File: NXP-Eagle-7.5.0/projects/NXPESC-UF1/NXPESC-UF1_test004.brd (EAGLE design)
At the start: 59.7 x 20.3 mm, 63 parts, among them J2 FLH1-03SZ-S3A-T, U1 MKV31F512VLL12-M, U10 PSMN1R4-30YLD, U11 PSMN1R4-30YLD, U12 PSMN1R4-30YLD, U13 PSMN1R4-30YLD, U2 MKV31F512VLH12-M, U8 PSMN1R4-30YLD, U9 PSMN1R4-30YLD

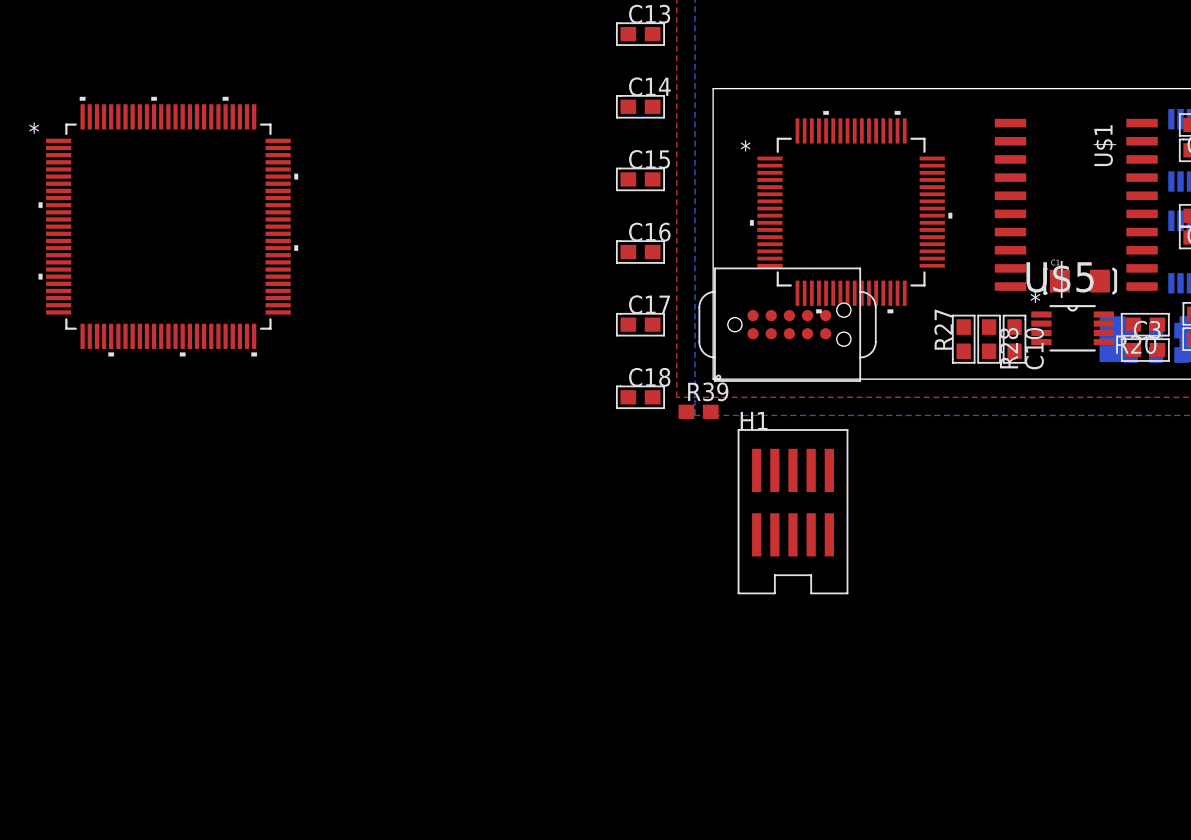
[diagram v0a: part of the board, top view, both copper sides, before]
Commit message: connected additional signals to gate driver
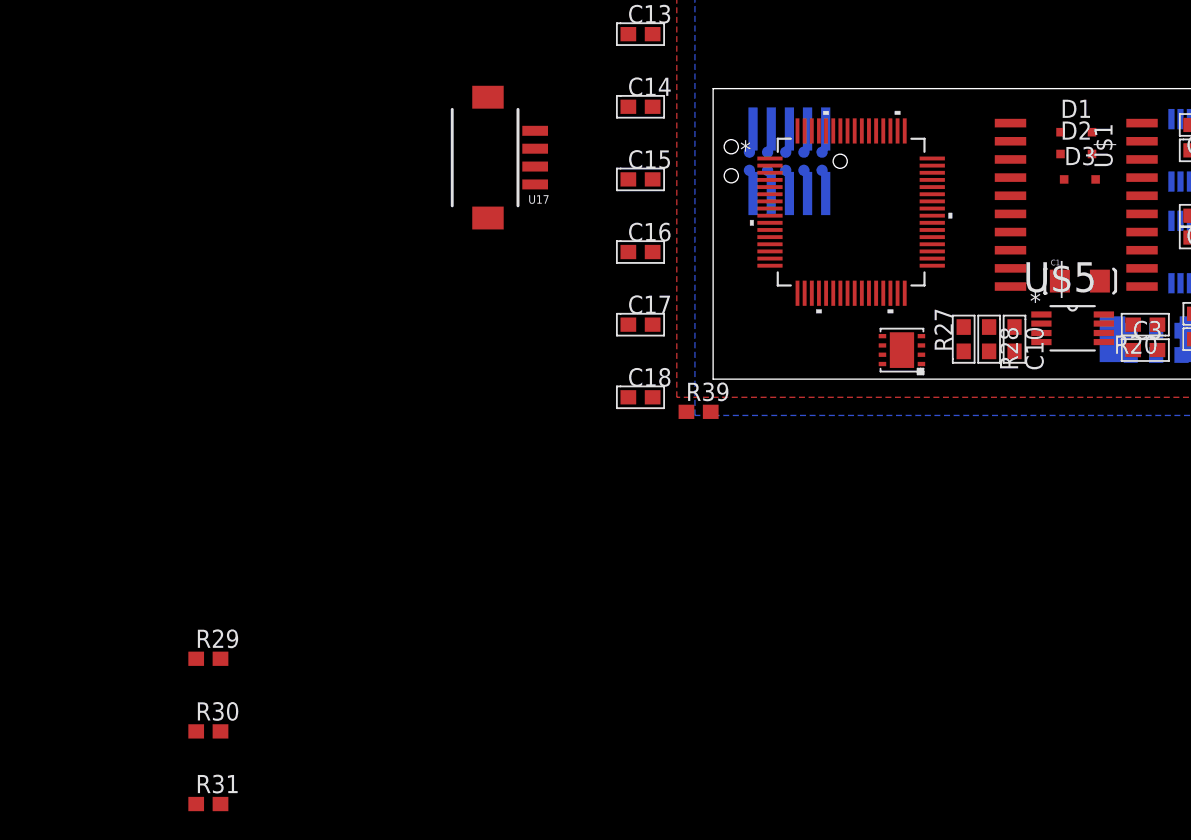
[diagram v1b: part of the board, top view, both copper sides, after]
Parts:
- removed U1: MKV31F512VLL12-M, MKV31F512VLL12:LQFP-100_14X14X1_7-M
- added D1, D2, D3: (no value), etc-diode_002a:SOD323-R
- added R29, R30, R31: RESC0603-100R, etc_rcl:C0603
- added U15: TJA1042TK/3, TJA1042T:HVSON8
- added U17: DF13-4P-1.25H, pixhawk2:DF13A-4P-1.25H
- C1: value (none) -> Find a 50V
- moved H1 23.9 mm to (5.33, 15.2), flipped to the bottom
- moved H3 13.6 mm to (8.89, 15.2), flipped to the bottom
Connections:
- net N$7 renamed PWM_BT
- net N$8 renamed PWM_BB
- removed net VB1: U$1.20
- removed net VB2: U$1.16
- removed net VB3: U$1.10
- removed net VDD_2: U2.30
- removed net VDD_3: U1.40, U2.48
- removed net VDD_7: U1.89
- removed net VSS_2: U2.31
- removed net VSS_3: U1.41
- removed net VSS_7: U1.88
- new net +5V: U15.3
- new net CAN0_RX: U15.4, U2.29
- new net CAN0_TX: U15.1, U2.28
- new net N$15: D3.C, U$1.20
- new net N$16: D2.C, U$1.16
- new net N$18: D1.C, U$1.10
- new net N$22: U15.7, U17.2
- new net N$23: U15.6, U17.3
- new net N$7: D3.A, R31.2
- new net N$8: R29.1, R30.1, R31.1
- new net PWM_AB: U$1.2, U2.45
- new net PWM_AT: U$1.1, U2.44
- new net PWM_CB: U$1.6, U2.62
- new net PWM_CT: U$1.5, U2.61
- new net STB: U15.8, U2.27
- net +3V3: now also U15.5, U2.30, U2.48; no longer U1.30, U1.48, U1.61, U1.75, U1.8, U2.20, U2.47
- net GND: now also U15.2, U17.4, U2.31, U2.47; no longer U1.29, U1.49, U1.60, U1.74, U1.9, U2.21, U2.32
- net N$5: now also D1.A, R29.2; no longer U$1.1, U1.71, U2.44
- net N$6: now also D2.A, R30.2; no longer U$1.2, U1.72, U2.45
- net VDDA: no longer U1.22
- net VREFH: no longer U1.23
- net VREFL: no longer U1.24
- net VSSA: no longer U1.25

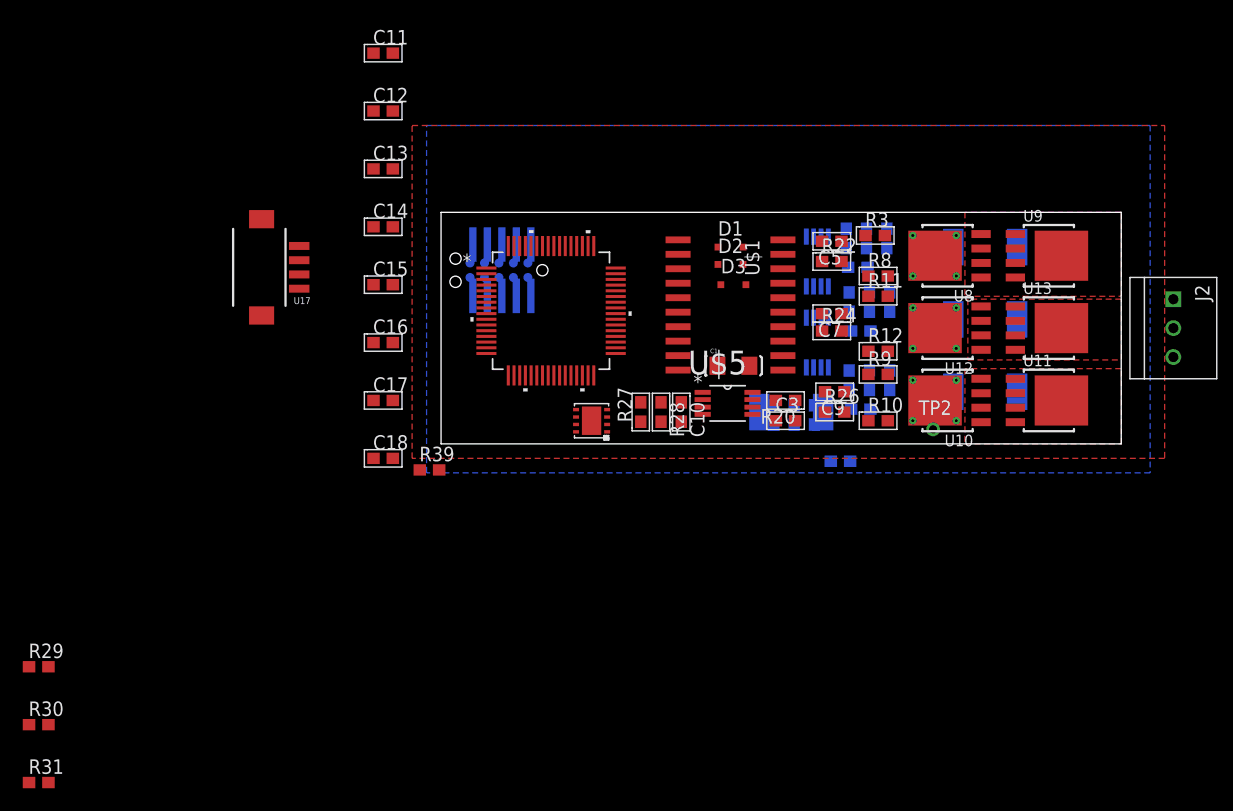
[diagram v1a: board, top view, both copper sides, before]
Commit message: moved from rev 003 to 004, merged in Gallowaa CAN conenctor additions.
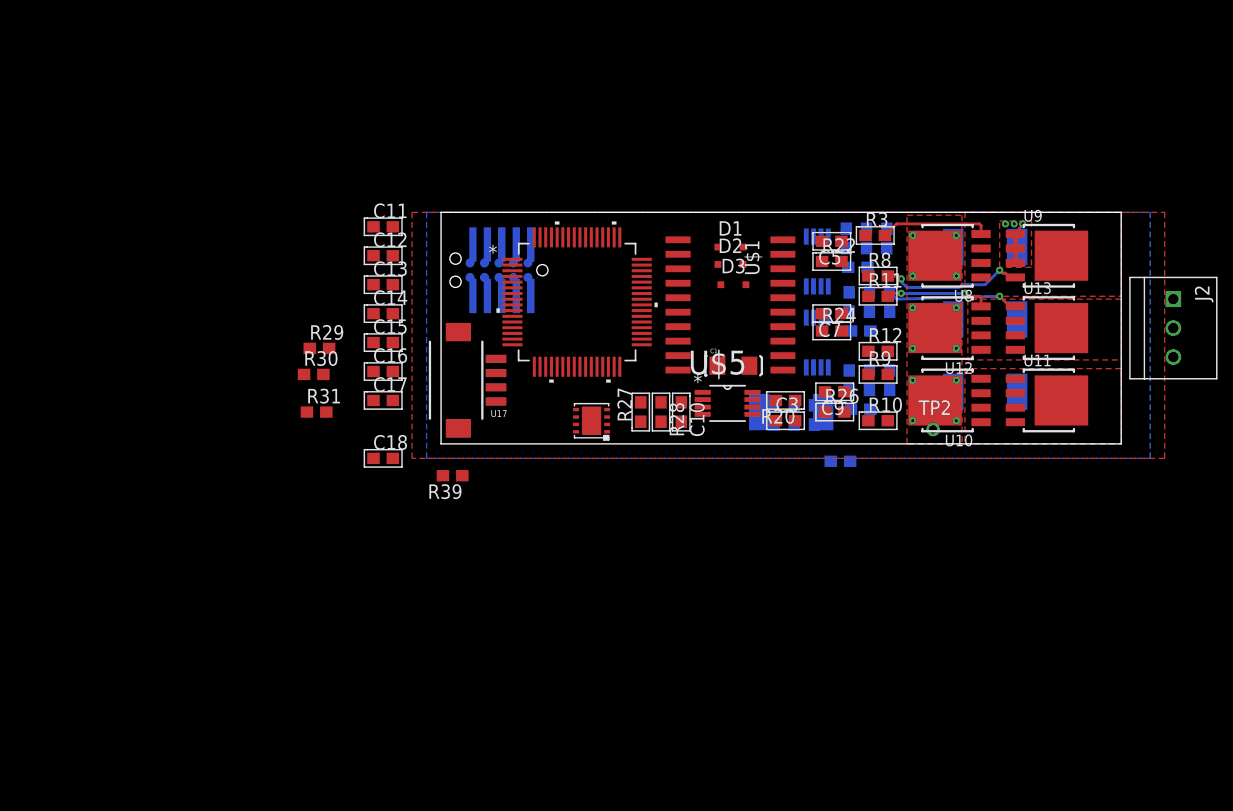
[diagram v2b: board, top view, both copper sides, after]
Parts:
- added U1: DF13-4P-1.25H, pixhawk2:DF13A-4P-1.25H
- moved R31 40.6 mm to (-10.9, 2.79)
- moved R30 39.1 mm to (-11.2, 6.10)
- moved R29 37.3 mm to (-10.7, 8.38)
- moved U17 19.9 mm to (1.52, 5.59)
- moved C11 15.2 mm to (-5.08, 19.1)
- moved C12 12.7 mm to (-5.08, 16.5)
- moved C13 10.2 mm to (-5.08, 14.0)
- moved C14 7.62 mm to (-5.08, 11.4)
- moved C15 5.08 mm to (-5.08, 8.89)
- moved C16 2.54 mm to (-5.08, 6.35)
- moved U2 2.41 mm to (11.9, 12.4)
- moved R39 2.09 mm to (1.02, -2.79), turned to 180 degrees
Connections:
- removed net N$22: U15.7, U17.2
- removed net N$23: U15.6, U17.3
- new net CANH: U1.2, U15.7, U17.2
- new net CANL: U1.3, U15.6, U17.3
- net +5V: now also U1.1, U17.1
- net GND: now also U1.4
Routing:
- net N$3: track 0.00 -> 12.7 mm, vias 0 -> 2
- net N$12: track 0.00 -> 11.6 mm, vias 0 -> 1
- net N$1: track 0.00 -> 9.66 mm
- net N$10: track 0.00 -> 9.20 mm, vias 0 -> 2
- net N$2: track 0.00 -> 5.49 mm, vias 0 -> 3
- added copper zone on layer 1, net +V_MOTOR
- added copper zone on layer 1, net N$2

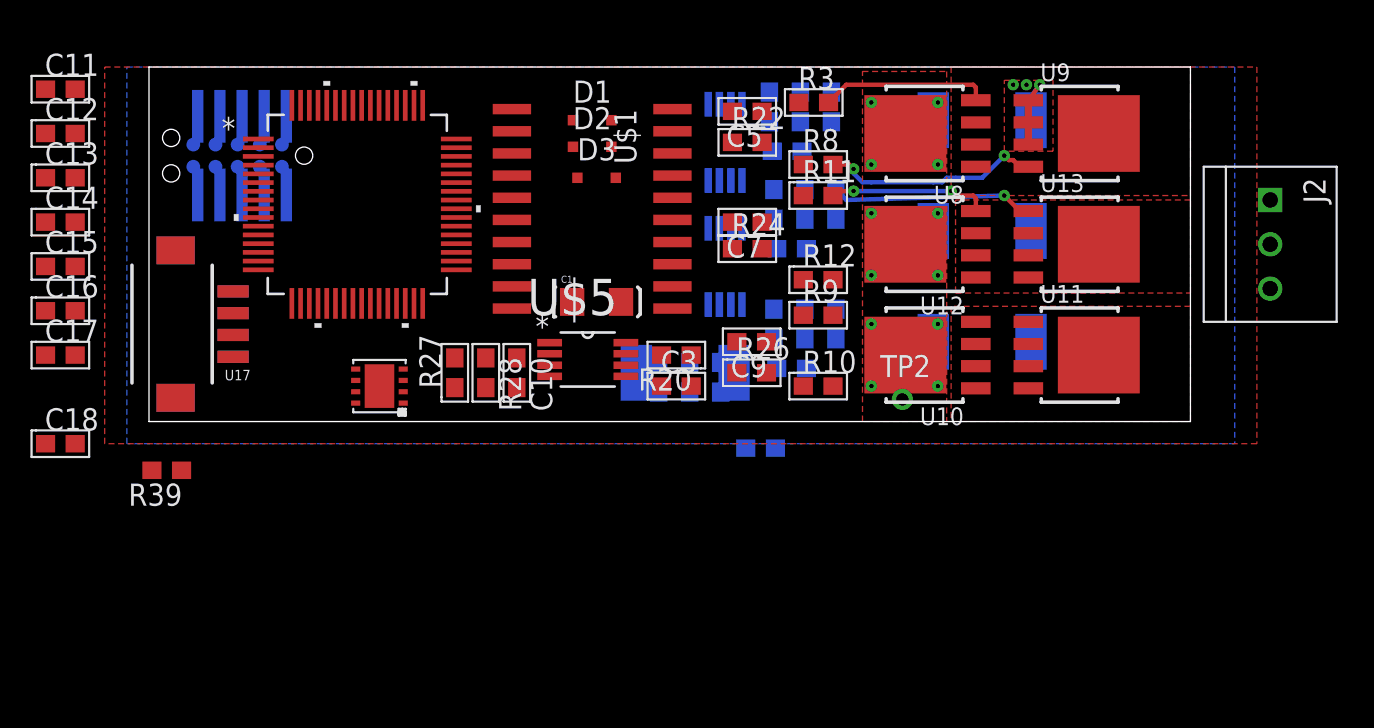
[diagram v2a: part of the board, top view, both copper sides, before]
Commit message: more test routing. layout is tight but looks possible. Need to switch back to schematic to add missing parts (regulators, connectors, capacitors.)
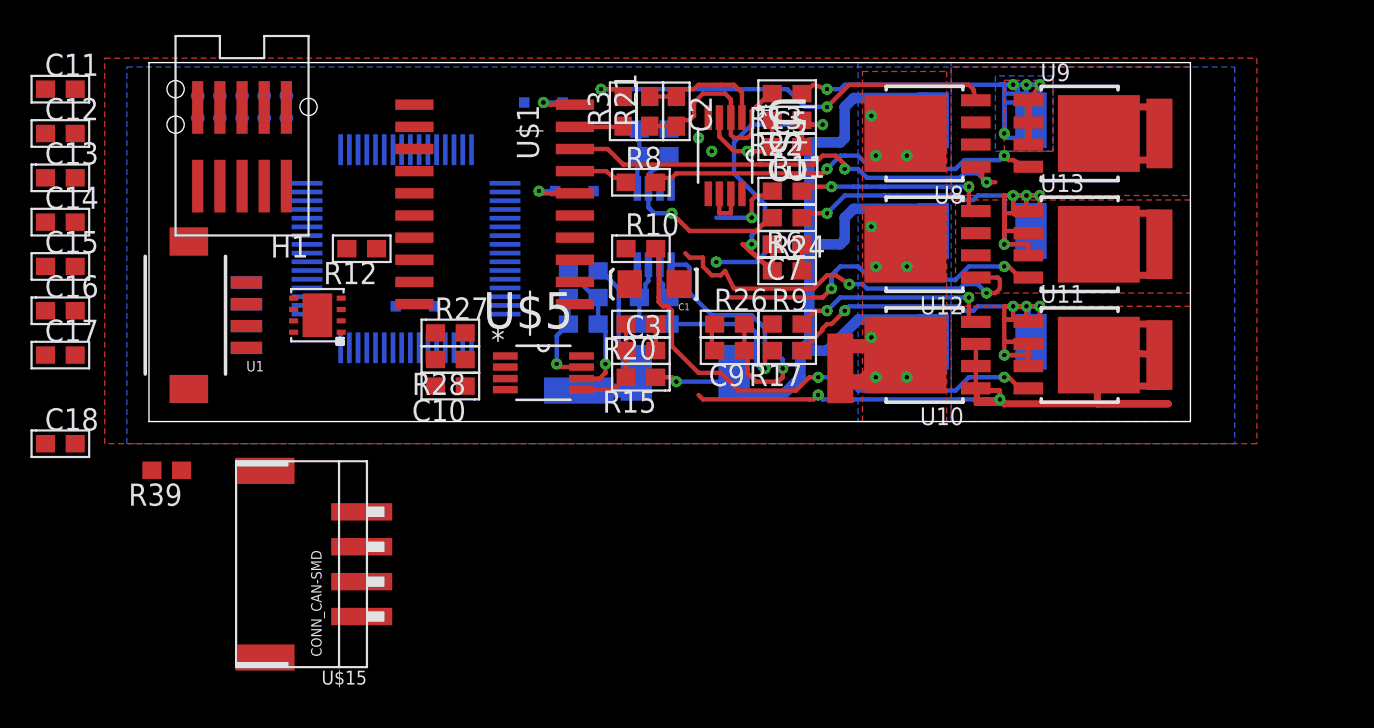
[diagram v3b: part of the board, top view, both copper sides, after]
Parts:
- removed J2: FLH1-03SZ-S3A-T, etc-connector-003a:J3
- removed TP2: +V_MOTOR, etc-connector-003a:TP-SMLL
- added P1, P2, P3, P4, P5: MOT_PWR_PAD-1, NXPHLITE:MPAD1
- added U$15: CONN_CAN-SMD, pixhawk2:S4B-PH-SM4-TB
- moved R12 26.2 mm to (12.2, 9.91), turned to 180 degrees
- moved D1 14.7 mm to (15.2, 6.60), flipped to the bottom, turned to 180 degrees
- moved R10 12.9 mm to (28.2, 9.91)
- moved R3 10.9 mm to (27.2, 17.8), turned to 90 degrees
- moved R8 10.2 mm to (28.2, 13.7)
- moved R16 9.96 mm to (24.9, 8.64), turned to 0 degrees
- moved R23 9.08 mm to (29.0, 15.2), turned to 0 degrees
- moved C8 8.77 mm to (29.0, 7.11), turned to 180 degrees
- moved R21 8.64 mm to (28.7, 17.8), flipped to the top
- moved C6 8.10 mm to (29.0, 16.8), turned to 180 degrees
- moved R15 7.97 mm to (28.2, 2.54), flipped to the top
- moved C4 7.62 mm to (24.9, 7.11), turned to 180 degrees
- moved R25 6.86 mm to (29.0, 5.59), turned to 0 degrees
- moved U$1 5.59 mm to (19.8, 12.4)
- moved U15 5.40 mm to (9.65, 6.10)
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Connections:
- net +V_MOTOR: now also P5.P$1; no longer TP2.1
- net AGND: now also P4.P$1
- net PH_A: now also P1.P$1; no longer J2.1
- net PH_B: now also P2.P$1; no longer J2.2
- net PH_C: now also P3.P$1; no longer J2.3
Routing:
- net CS_ABC_L/DCB_H: track 0.00 -> 61.7 mm, vias 0 -> 1
- net PH_B: track 0.00 -> 61.5 mm, vias 0 -> 2
- net PH_A: track 0.00 -> 40.4 mm, vias 0 -> 2
- net N$11: track 0.00 -> 39.5 mm, vias 0 -> 5
- net PH_C: track 0.00 -> 38.0 mm, vias 0 -> 2
- net N$12: track 11.6 -> 45.5 mm, vias 1 -> 5
- net N$2: track 5.49 -> 37.0 mm, vias 3 -> 5
- net ADC_MID: track 0.00 -> 30.6 mm, vias 0 -> 2
- net N$9: track 0.00 -> 28.9 mm, vias 0 -> 2
- net N$17: track 0.00 -> 20.7 mm, vias 0 -> 2
- net CS_B_L: track 0.00 -> 16.2 mm, vias 0 -> 1
- net N$1: track 9.66 -> 25.6 mm, vias 0 -> 2
- net CS_B_H: track 0.00 -> 12.9 mm, vias 0 -> 1
- net CS_A_H: track 0.00 -> 12.4 mm
- net N$4: track 0.00 -> 11.9 mm, vias 0 -> 2
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- added copper zone on layer 16, net +V_MOTOR
- added copper zone on layer 16, net N$2
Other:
- board size 59.7 x 20.3 mm -> 59.7 x 20.6 mm
